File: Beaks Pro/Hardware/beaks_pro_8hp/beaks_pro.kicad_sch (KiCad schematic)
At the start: 3 parts, among them J1 Pins_02x10_P2.54mm_TH, J14 Pins_02x10_P2.54mm_TH

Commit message: Layout done on 8HP SMT version
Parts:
- removed J1, J14: Pins_02x10_P2.54mm_TH, Connector_PinHeader_2.54mm:PinHeader_2x10_P2.54mm_Vertical, symbol PCM_4ms_Connector:Pins_02x10_P1.27mm_TH
- added J1: Conn_02x08_Odd_Even, Connector_PinSocket_2.54mm:PinSocket_2x08_P2.54mm_Vertical, symbol Connector_Generic:Conn_02x08_Odd_Even
- added J14: Conn_02x12_Odd_Even, Connector_PinSocket_2.54mm:PinSocket_2x12_P2.54mm_Vertical, symbol Connector_Generic:Conn_02x12_Odd_Even
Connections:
- net -10V_REF: now also J14.4 (Pin_4)
- net CV1_ATVPOT: now also J14.5 (Pin_5)
- net CV1_JACK: now also J14.3 (Pin_3)
- net CV1_POT: now also J14.7 (Pin_7)
- net CV2_ATVPOT: now also J14.11 (Pin_11)
- net CV2_JACK: now also J14.9 (Pin_9)
- net CV2_POT: now also J14.13 (Pin_13)
- net CV3_ATVPOT: now also J14.17 (Pin_17)
- net CV3_JACK: now also J14.15 (Pin_15)
- net CV3_POT: now also J14.18 (Pin_18)
- net CV4_ATVPOT: now also J14.14 (Pin_14)
- net CV4_JACK: now also J14.16 (Pin_16)
- net CV4_POT: now also J14.12 (Pin_12)
- net GND: now also J1.10 (Pin_10), J1.12 (Pin_12), J1.15 (Pin_15), J14.1 (Pin_1), J14.19 (Pin_19), J14.2 (Pin_2), J14.20 (Pin_20), J14.6 (Pin_6)
- net LED1: now also J1.5 (Pin_5)
- net LED2: now also J1.7 (Pin_7)
- net LED3: now also J1.9 (Pin_9)
- net LED4: now also J1.11 (Pin_11)
- net LED5: now also J1.13 (Pin_13)
- net LED_SALIDA_1: now also J1.1 (Pin_1)
- net LED_SALIDA_2: now also J1.3 (Pin_3)
- net OUT1: now also J1.14 (Pin_14)
- net OUT1_ATVPOT: now also J14.23 (Pin_23)
- net OUT2: now also J1.16 (Pin_16)
- net OUT2_ATVPOT: now also J14.24 (Pin_24)
- net PRE_ATV_OUT1: now also J14.21 (Pin_21)
- net PRE_ATV_OUT2: now also J14.22 (Pin_22)
- net SW_DUAL: now also J1.2 (Pin_2)
- net SW_MODE: now also J1.4 (Pin_4)
- net SW_TRIG1: now also J1.6 (Pin_6)
- net SW_TRIG2: now also J1.8 (Pin_8)
- net TRIG_1: now also J14.8 (Pin_8)
- net TRIG_2: now also J14.10 (Pin_10)
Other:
- note removed: "Board-to-board Interface"

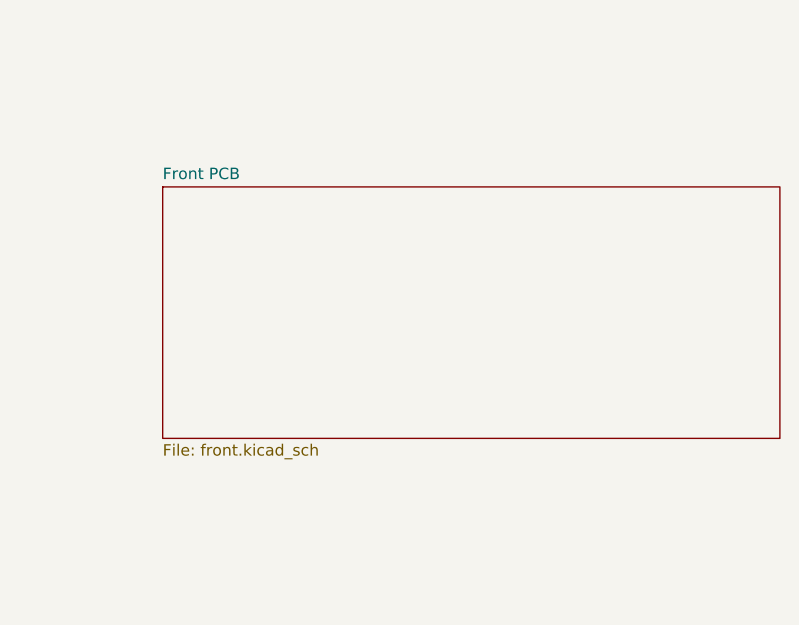
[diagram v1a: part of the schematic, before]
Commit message: Split 8HP design up in separate files, for SMT export. Add step file export
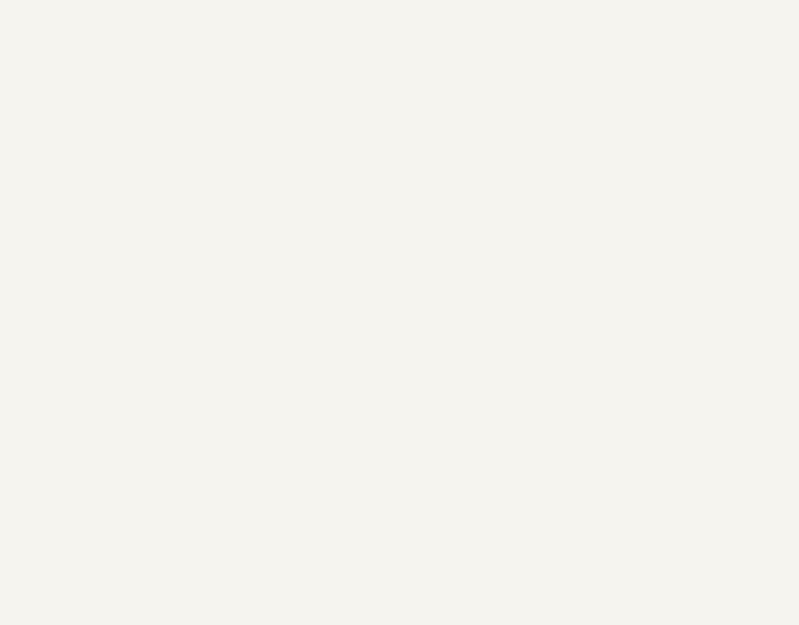
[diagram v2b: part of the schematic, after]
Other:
- removed sheet Front PCB
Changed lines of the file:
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@@
-	)
-	(sheet
-		(at 210.82 132.08)
-		(size 68.58 27.94)
-		(fields_autoplaced yes)
-		(stroke
-			(width 0.1524)
-			(type solid)
-		)
-		(fill
-			(color 0 0 0 0.0000)
-		)
-		(property "Sheetname" "Front PCB"
-			(at 210.82 131.3684 0)
-			(effects
-				(font
-					(size 1.27 1.27)
-				)
-				(justify left bottom)
-			)
-		)
-		(property "Sheetfile" "front.kicad_sch"
-			(at 210.82 160.6046 0)
-			(effects
-				(font
-					(size 1.27 1.27)
-				)
-				(justify left top)
-			)
-		)
-		(instances
-			(project "beaks_pro"
-				(path "/42239145-e5b3-41f8-a147-63fb75708e52"
-					(page "6")
-				)
-			)
-		)
 	)
 	(sheet
